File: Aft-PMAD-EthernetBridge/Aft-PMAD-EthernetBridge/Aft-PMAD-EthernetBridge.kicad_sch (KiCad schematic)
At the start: 0 parts

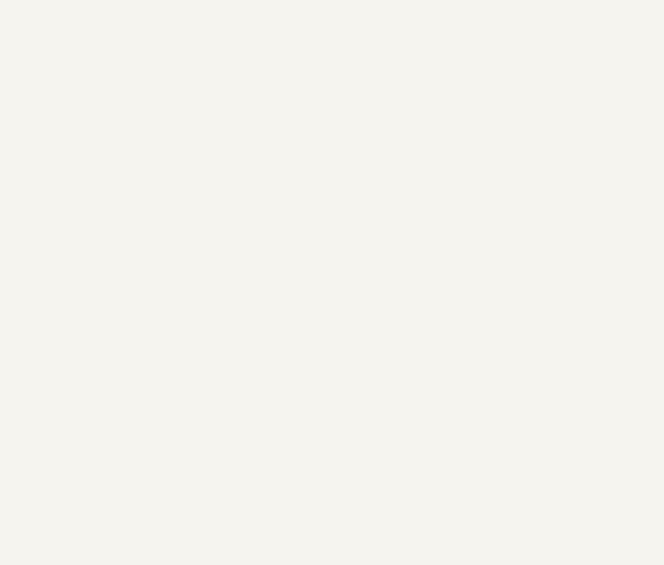
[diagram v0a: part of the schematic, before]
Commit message: ADD 5V stepdown
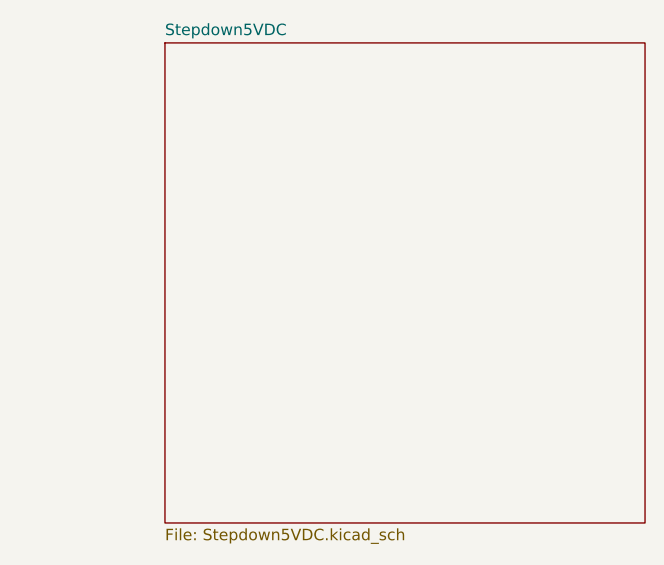
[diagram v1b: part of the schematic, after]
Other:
- added sheet Stepdown5VDC (Stepdown5VDC.kicad_sch)
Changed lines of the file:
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@@
 	(paper "B")
+	(sheet
+		(at 133.35 38.1)
+		(size 53.34 53.34)
+		(exclude_from_sim no)
+		(in_bom yes)
+		(on_board yes)
+		(dnp no)
+		(fields_autoplaced yes)
+		(stroke
+			(width 0.1524)
+			(type solid)
+		)
+		(fill
+			(color 0 0 0 0)
+		)
+		(property "Sheetname" "Stepdown5VDC"
+			(at 133.35 37.3884 0)
+			(show_name no)
+			(do_not_autoplace no)
+			(effects
+				(font
+					(size 1.27 1.27)
+				)
+				(justify left bottom)
+			)
+		)
+		(property "Sheetfile" "Stepdown5VDC.kicad_sch"
+			(at 133.35 92.0246 0)
+			(show_name no)
+			(do_not_autoplace no)
+			(effects
+				(font
+					(size 1.27 1.27)
+				)
+				(justify left top)
+			)
+		)
+		(instances
+			(project "Aft-PMAD-EthernetBridge"
+				(path "/2d9655a2-9a74-4f5c-bab7-1e19113f649a"
+					(page "3")
+				)
+			)
+		)
+	)
 	(sheet
 		(at 50.8 38.1)

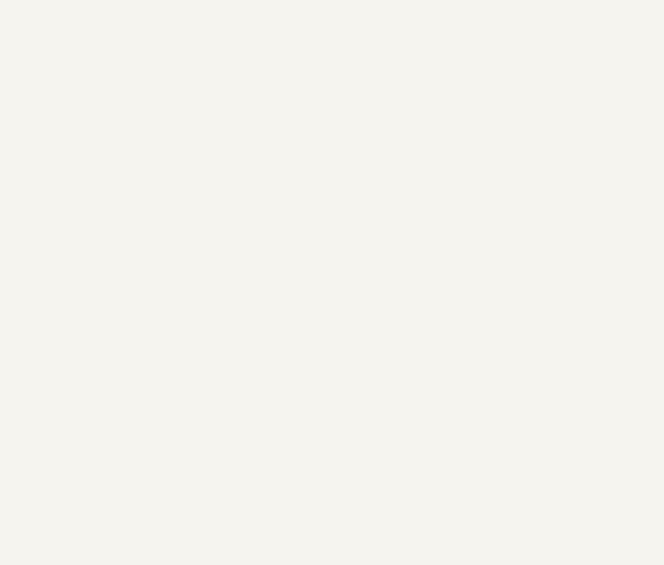
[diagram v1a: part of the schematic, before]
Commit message: start 3v3 Stepdown3V3.kicad_sch
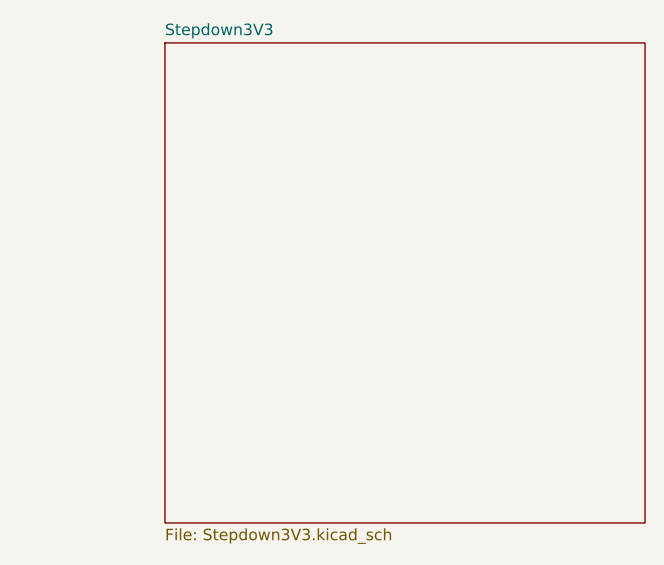
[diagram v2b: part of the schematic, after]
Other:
- added sheet Stepdown3V3 (Stepdown3V3.kicad_sch)
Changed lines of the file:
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@@
 	(paper "B")
+	(sheet
+		(at 217.17 38.1)
+		(size 53.34 53.34)
+		(exclude_from_sim no)
+		(in_bom yes)
+		(on_board yes)
+		(dnp no)
+		(fields_autoplaced yes)
+		(stroke
+			(width 0.1524)
+			(type solid)
+		)
+		(fill
+			(color 0 0 0 0)
+		)
+		(property "Sheetname" "Stepdown3V3"
+			(at 217.17 37.3884 0)
+			(show_name no)
+			(do_not_autoplace no)
+			(effects
+				(font
+					(size 1.27 1.27)
+				)
+				(justify left bottom)
+			)
+		)
+		(property "Sheetfile" "Stepdown3V3.kicad_sch"
+			(at 217.17 92.0246 0)
+			(show_name no)
+			(do_not_autoplace no)
+			(effects
+				(font
+					(size 1.27 1.27)
+				)
+				(justify left top)
+			)
+		)
+		(instances
+			(project "Aft-PMAD-EthernetBridge"
+				(path "/2d9655a2-9a74-4f5c-bab7-1e19113f649a"
+					(page "4")
+				)
+			)
+		)
+	)
 	(sheet
 		(at 133.35 38.1)
